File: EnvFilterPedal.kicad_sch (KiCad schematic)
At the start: 114 parts, among them J101 ScopeGroundLoop, J102 IO, Q101 BC857, Q102 BC857, Q103 BC847, U101 TL074, U102 TL074, U103 TL074, U104 LM13700, U105 AZ34063U

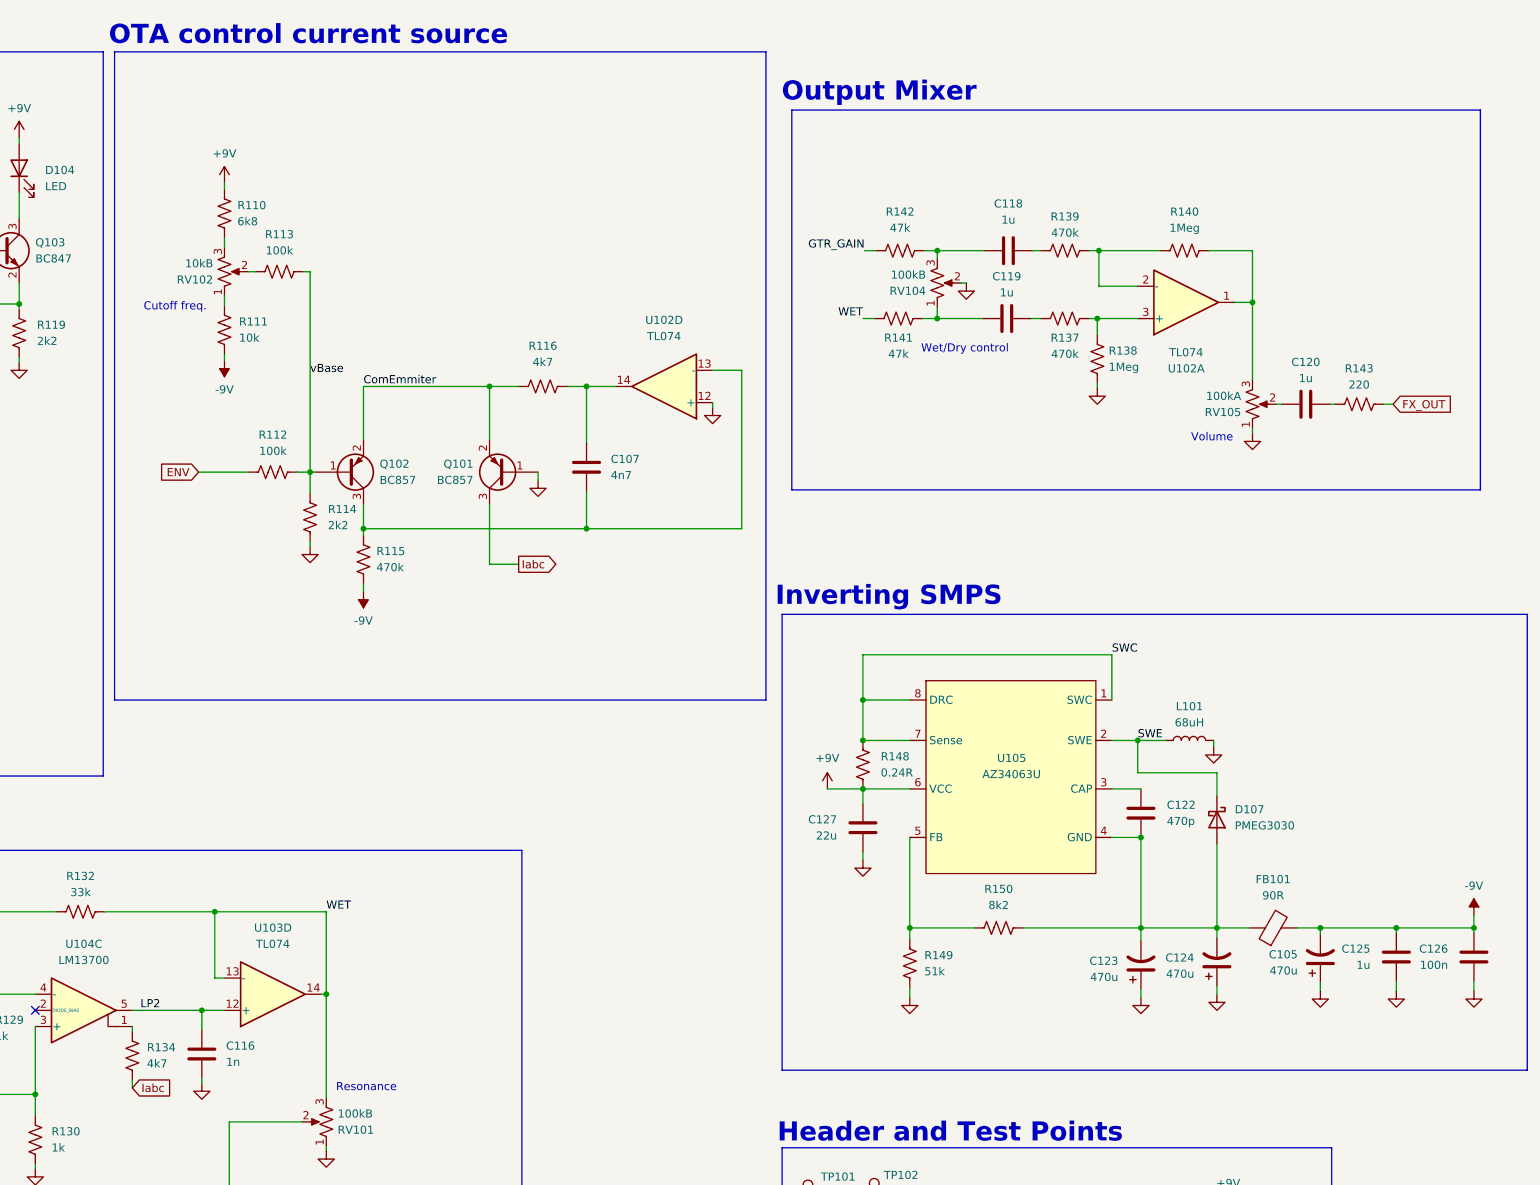
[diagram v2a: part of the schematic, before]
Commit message: added SMPS input filtering
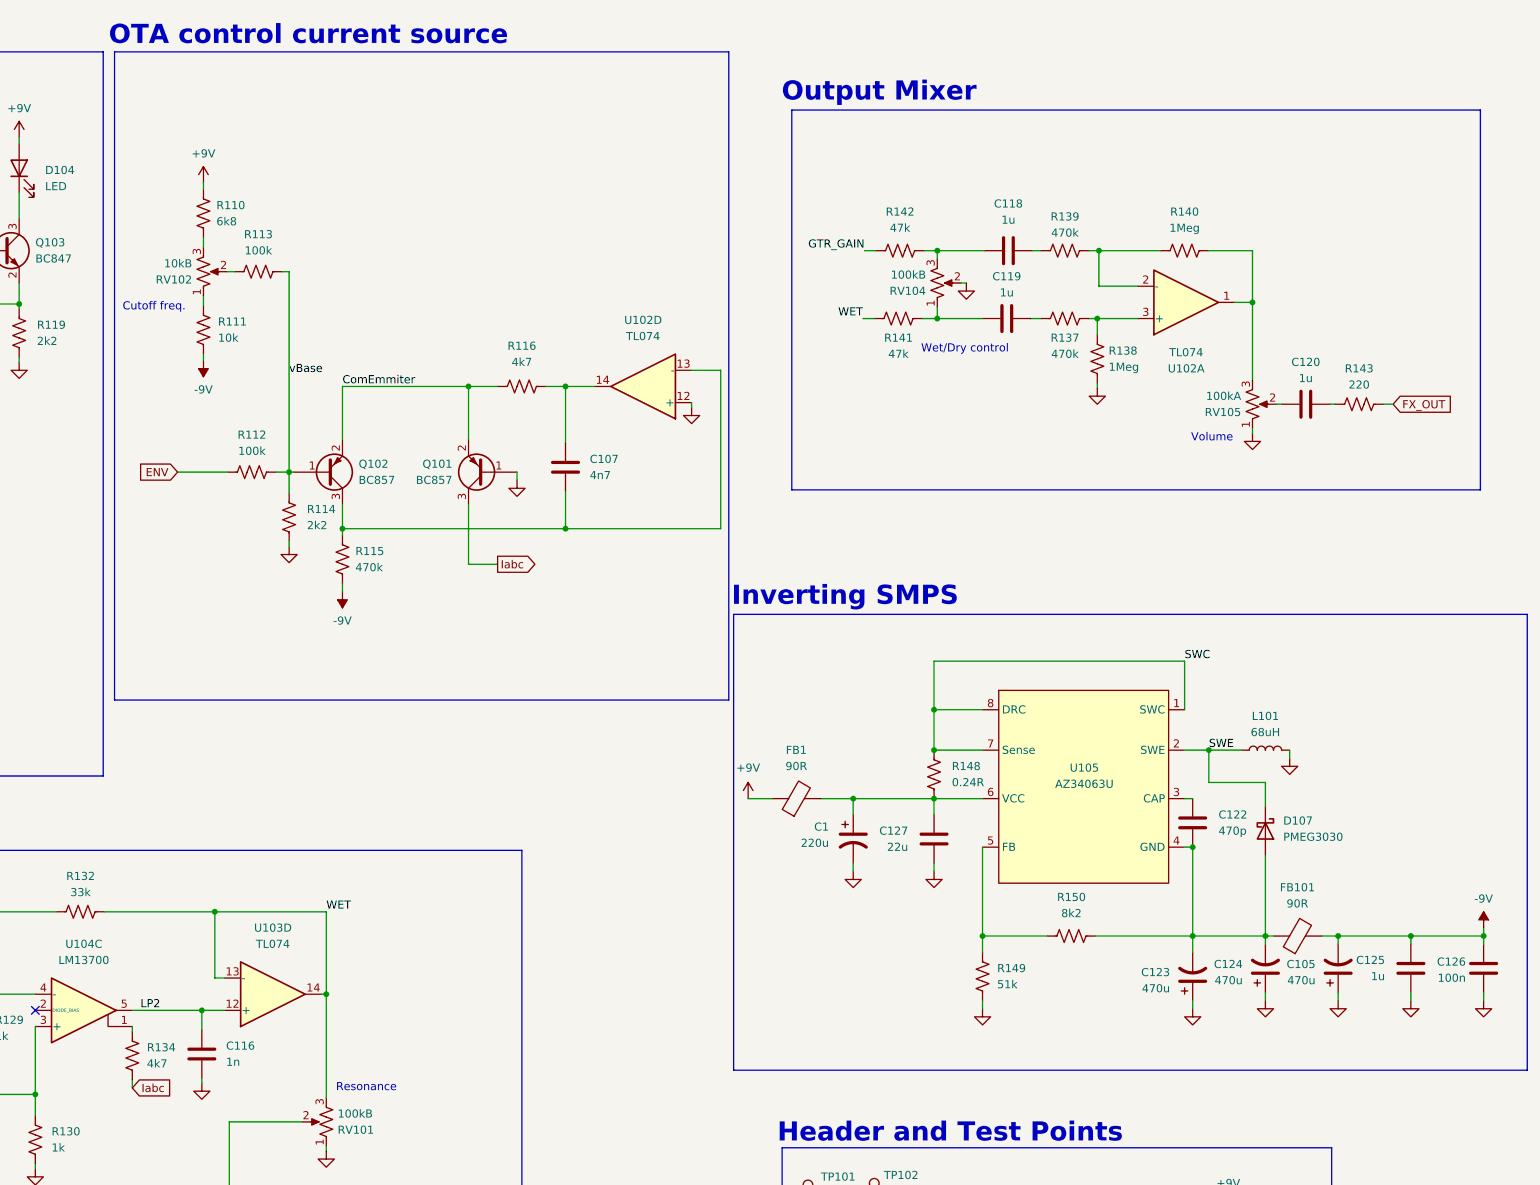
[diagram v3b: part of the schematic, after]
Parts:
- added C1: 220u, Capacitor_THT:CP_Radial_D5.0mm_P2.00mm, symbol Device:C_Polarized_US
- added FB1: 90R, Inductor_SMD:L_0805_2012Metric, symbol Device:FerriteBead
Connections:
- net +9V: now also FB1.1; no longer C127.1, R148.1, U105.6 (VCC)
- net GND: now also C1.2
- new net: C1.1, C127.1, FB1.2, R148.1, U105.6 (VCC)
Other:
- moved on the sheet: C105, C107, C122, C123, C124, C125, C126, C127, D107, FB101, L101, Q101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

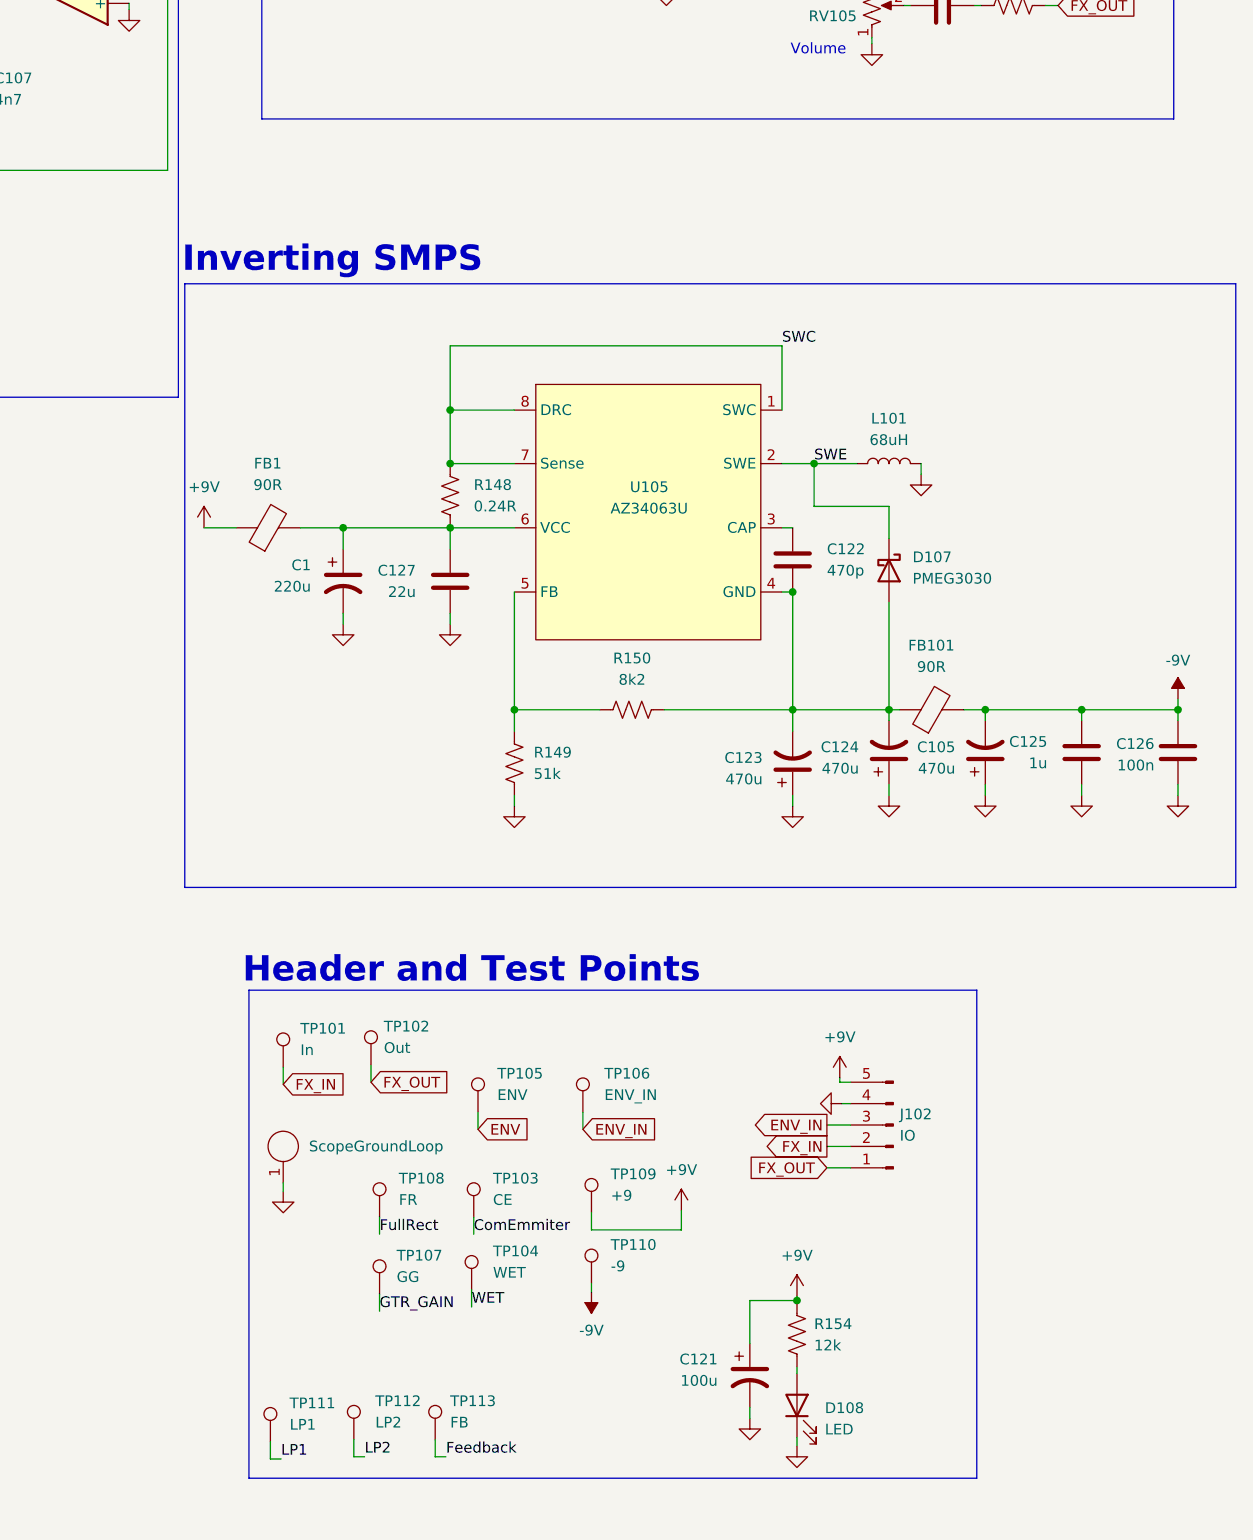
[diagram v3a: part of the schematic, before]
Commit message: switched to 1u inductor on SMPS output
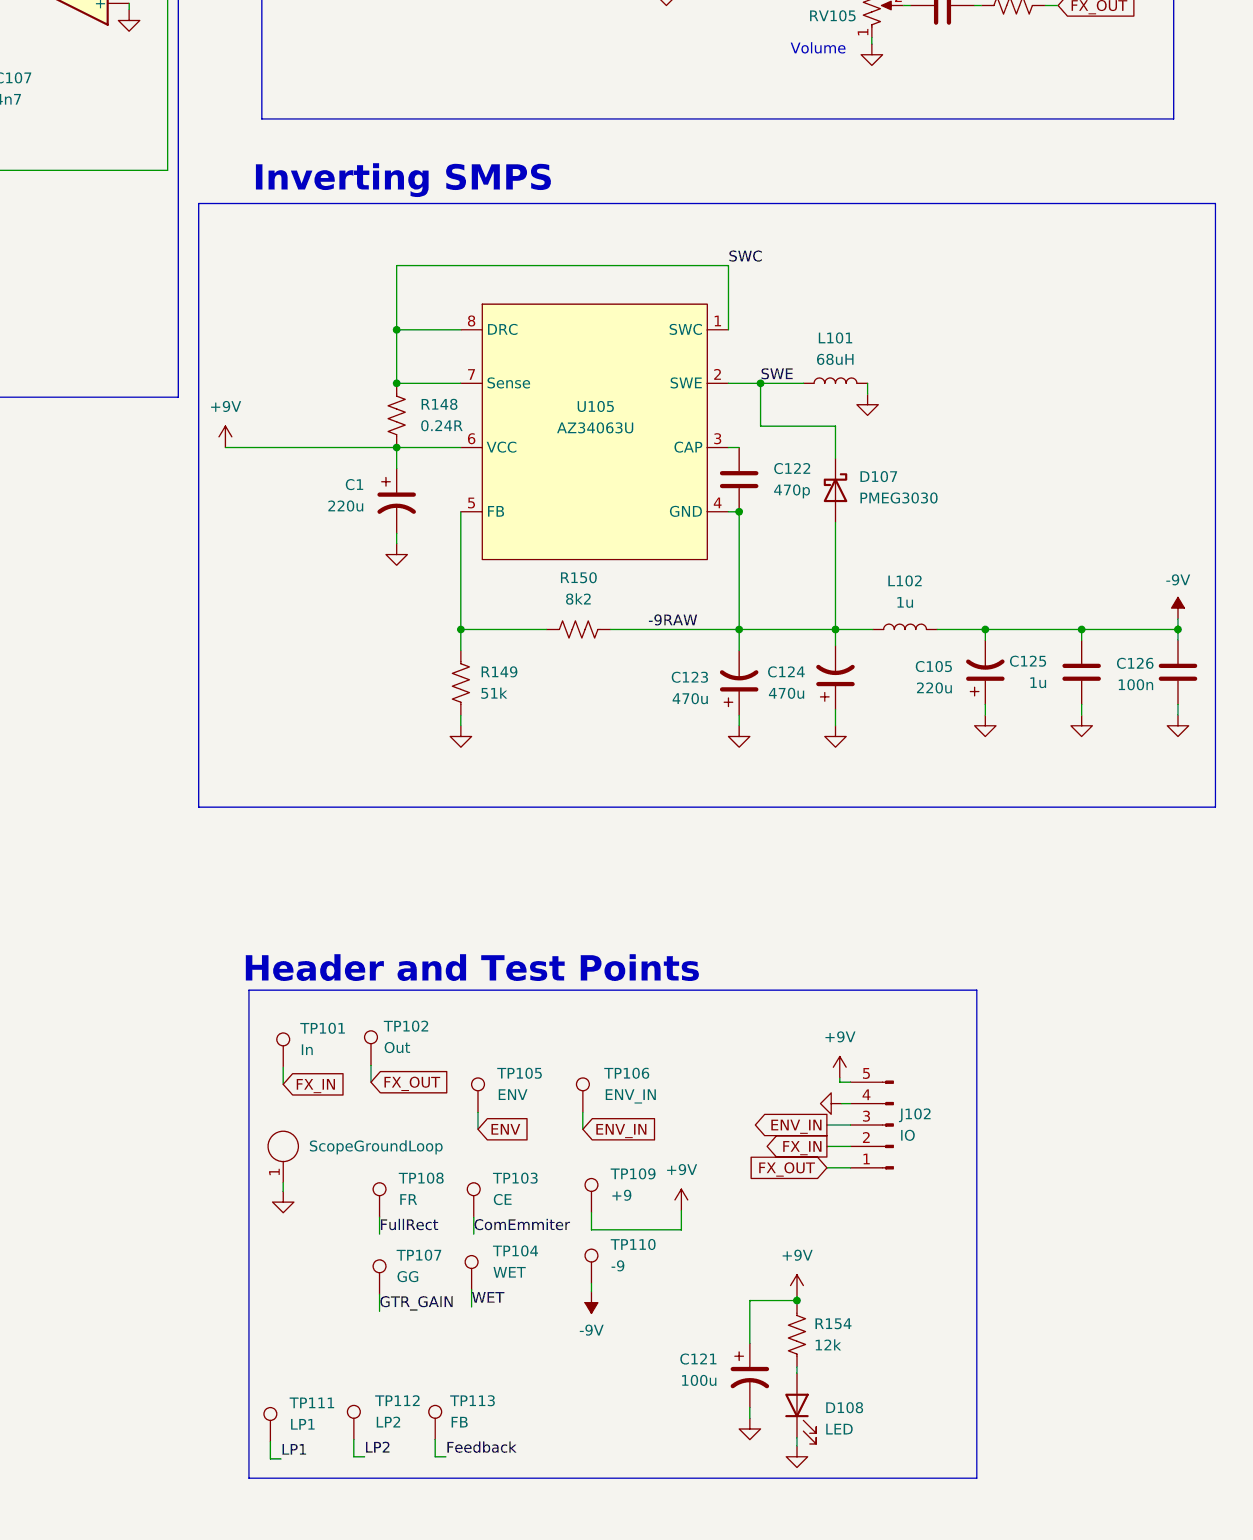
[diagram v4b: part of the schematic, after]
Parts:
- removed C127: 22u, Capacitor_SMD:C_0805_2012Metric, symbol Device:C
- removed FB1, FB101: 90R, Inductor_SMD:L_0805_2012Metric, symbol Device:FerriteBead
- added L102: 1u, Inductor_SMD:L_0805_2012Metric, symbol Device:L
- C105: value 470u -> 220u
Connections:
- net +9V: now also C1.1, R148.1, U105.6 (VCC)
- net -9V: now also L102.2
- net -9RAW: now reaches C122.2, C123.2, C124.2, D107.2 (A), R150.2, U105.4 (GND)
- net -9RAW: now also L102.1
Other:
- moved on the sheet: C1, C105, C122, C123, C124, C125, C126, D107, L101, R148, R149, R150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

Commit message: new layout
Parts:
- removed C126: 100n, Capacitor_SMD:C_0805_2012Metric, symbol Device:C
- removed D105, D106: LED, LED_THT:LED_D3.0mm, symbol Device:LED
- removed R101: 100k, Resistor_SMD:R_0805_2012Metric, symbol Device:R_US
- added TP14: -9R, TestPoint:TestPoint_THTPad_D2.0mm_Drill1.0mm_VAL, symbol Connector:TestPoint
- C21: renamed from C123; value 470u -> 220u; now not fitted
- C26: renamed from C125; value 1u -> 10u
- D4: renamed from D109; now fitted
- D5: renamed from D110; now fitted
- J1: renamed from J101; footprint Connector:THT_GND_WIRE -> Connector_Pin:THT_GND_WIRE
- L2: renamed from L102; value 1u -> 4u7; footprint Inductor_SMD:L_0805_2012Metric -> Inductor_SMD:L_Bourns_SRP3212
- R10: renamed from R102; value 100k -> 47k
- RV1: renamed from RV103; footprint Potentiometer_THT:Potentiometer_Alpha_RV16AF_42_VeryLong -> Potentiometer_THT:Potentiometer_Alpha_RV16AF_42_Single_Long
- RV2: renamed from RV102; footprint Potentiometer_THT:Potentiometer_Alpha_RV16AF_42_VeryLong -> Potentiometer_THT:Potentiometer_Alpha_RV16AF_42_Single_Long
- RV3: renamed from RV101; footprint Potentiometer_THT:Potentiometer_Alpha_RV16AF_42_VeryLong -> Potentiometer_THT:Potentiometer_Alpha_RV16AF_42_Single_Long
- RV4: renamed from RV104; footprint Potentiometer_THT:Potentiometer_Alpha_RV16AF_42_VeryLong -> Potentiometer_THT:Potentiometer_Alpha_RV16AF_42_Single_Long
- RV5: renamed from RV105; footprint Potentiometer_THT:Potentiometer_Alpha_RV16AF_42_VeryLong -> Potentiometer_THT:Potentiometer_Alpha_RV16AF_42_Single_Long
- renumbered C102 to C1, C115 to C10, C104 to C11, C113 to C12, C110 to C13, C117 to C14, C116 to C15, C107 to C16, C1 to C17, C118 to C18, C119 to C19, C101 to C2, C122 to C20, C124 to C22, C120 to C23, C105 to C24, C121 to C25, C106 to C3, C108 to C4, C103 to C5, C109 to C6, C111 to C7, C112 to C8, C114 to C9, D101 to D1, D102 to D2, D103 to D3, D104 to D6, D107 to D7, D108 to D8, J102 to J2, L101 to L1, Q103 to Q1, Q102 to Q2, Q101 to Q3, R104 to R1, R120 to R11, R107 to R12, R127 to R13, R103 to R14, R125 to R15, R124 to R16, R126 to R17, R128 to R18, R133 to R19, R121 to R2, R109 to R20, R108 to R21, R135 to R22, R131 to R23, R129 to R24, R119 to R25, R136 to R26, R130 to R27, R132 to R28, R134 to R29, R117 to R3, R110 to R30, R111 to R31, R112 to R32, R113 to R33, R114 to R34, R115 to R35, R116 to R36, R148 to R37, R141 to R38, R142 to R39, R123 to R4, R149 to R40, R150 to R41, R139 to R42, R137 to R43, R138 to R44, R140 to R45, R143 to R46, R154 to R47, R105 to R5, R122 to R6, R118 to R7, R106 to R8, TP111 to TP1, TP105 to TP10, TP106 to TP11, TP109 to TP12, TP110 to TP13, TP101 to TP2, TP112 to TP3, TP102 to TP4, TP108 to TP5, TP107 to TP6, TP113 to TP7, TP103 to TP8, TP104 to TP9, U101 to U1, U102 to U2, U103 to U3, U104 to U4, U105 to U5
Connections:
- net -9RAW: now also TP14.1
- no-connect marks 5 -> 6
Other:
- moved on the sheet: C25, D8, J2, R47
